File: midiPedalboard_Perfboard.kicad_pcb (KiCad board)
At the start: 8 copper layers, 66 x 50.8 mm, 49 parts, among them J1 wire, J10 wire, J11 wire, J12 wire, J13 wire, J14 wire, J15 MIDI_4, J16 MIDI_5, J17 MIDI_4, J18 MIDI_2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

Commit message: fix internal rst wire
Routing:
- net Net-(U1-PadRST): track 15.3 -> 16.3 mm
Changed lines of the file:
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@@
     (thickness 1.6)
     (drawings 6)
-    (tracks 135)
+    (tracks 139)
     (zones 0)
     (modules 49)
@@
   (layers
     (0 F.Cu signal)
-    (1 In1.Cu signal hide)
-    (2 In2.Cu signal hide)
+    (1 In1.Cu signal)
+    (2 In2.Cu signal)
     (3 wire1 signal)
     (4 wire2 signal)
-    (5 wire3 signal hide)
-    (6 wire4 signal hide)
+    (5 wire3 signal)
+    (6 wire4 signal)
     (31 B.Cu signal)
     (33 F.Adhes user)
@@
   )
   (setup
-    (last_trace_width 0.5)
+    (last_trace_width 0.25)
     (user_trace_width 0.25)
     (user_trace_width 0.5)
@@
   (segment (start 157.48 109.22) (end 157.48 111.180248) (width 0.25) (layer wire2) (net 27))
   (segment (start 160.02 113.720248) (end 160.02 114.3) (width 0.25) (layer wire2) (net 27))
-  (segment (start 144.999918 101.953781) (end 144.999918 86.697781) (width 0.5) (layer In1.Cu) (net 30))
+  (segment (start 144.78 86.344) (end 144.78 90.17) (width 0.25) (layer In1.Cu) (net 30))
+  (segment (start 144.78 90.17) (end 146.05 91.44) (width 0.25) (layer In1.Cu) (net 30))
+  (segment (start 146.05 91.44) (end 146.05 97.79) (width 0.25) (layer In1.Cu) (net 30))
+  (segment (start 144.78 99.06) (end 144.78 101.6) (width 0.25) (layer In1.Cu) (net 30))
+  (segment (start 146.05 97.79) (end 144.78 99.06) (width 0.25) (layer In1.Cu) (net 30))
   (segment (start 152.619918 86.697781) (end 150.079918 86.697781) (width 0.5) (layer In1.Cu) (net 31))
   (segment (start 149.86 81.28) (end 149.86 78.74) (width 0.5) (layer B.Cu) (net 37))

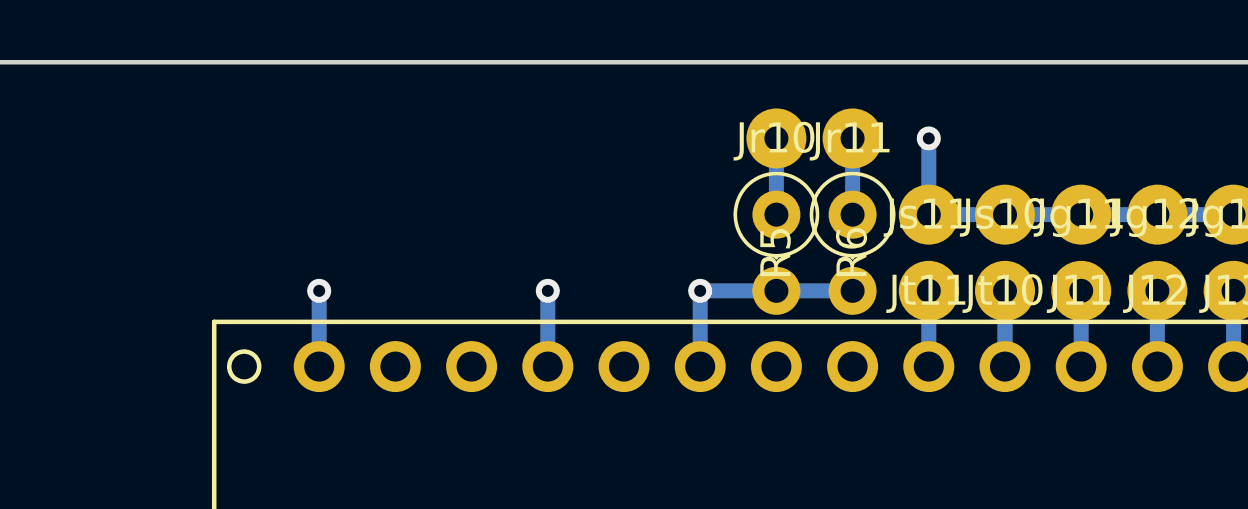
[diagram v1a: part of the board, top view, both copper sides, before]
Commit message: condensator for adc filtering
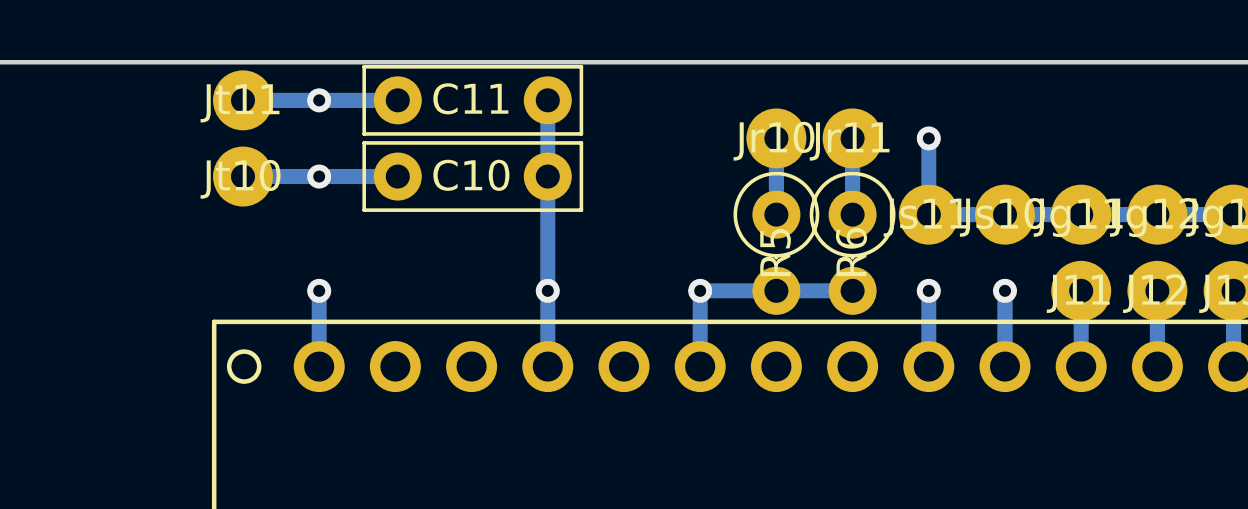
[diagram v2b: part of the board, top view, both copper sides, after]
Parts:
- added C10: 100n, Capacitor_THT:C_Rect_L7.0mm_W2.0mm_P5.00mm, F.Cu at (137.2, 80.0)
- added C11: 100n, Capacitor_THT:C_Rect_L7.0mm_W2.0mm_P5.00mm, F.Cu at (137.2, 77.5)
- moved Jt10 25.7 mm to (132.1, 80.0)
- moved Jt11 23.7 mm to (132.1, 77.5)
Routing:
- net /exp: track 2.52 -> 32.1 mm, vias 0 -> 2
- net /exp_2: track 2.52 -> 30.6 mm, vias 0 -> 2
- net GND: track 142.4 -> 148.8 mm
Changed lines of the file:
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@@
     (thickness 1.6)
     (drawings 6)
-    (tracks 139)
+    (tracks 162)
     (zones 0)
-    (modules 49)
+    (modules 51)
     (nets 40)
   )
@@
   )
   (setup
-    (last_trace_width 0.25)
+    (last_trace_width 0.5)
     (user_trace_width 0.25)
     (user_trace_width 0.5)
@@
   )
   (module Connector_Wire:SolderWirePad_1x01_Drill0.8mm (layer F.Cu)
-    (at 154.94 83.82 180)
+    (at 132.08 77.47 180)
     (descr "Wire solder connection")
     (tags connector)
@@
   )
   (module Connector_Wire:SolderWirePad_1x01_Drill0.8mm (layer F.Cu)
-    (at 157.48 83.82 180)
+    (at 132.08 80.01 180)
     (descr "Wire solder connection")
     (tags connector)
@@
     )
   )
+  (module Capacitor_THT:C_Rect_L7.0mm_W2.0mm_P5.00mm (layer F.Cu)
+    (at 137.24 80.01)
+    (descr "C, Rect series, Radial, pin pitch=5.00mm, , length*width=7*2mm^2, Capacitor")
+    (tags "C Rect series Radial pin pitch 5.00mm  length 7mm width 2mm Capacitor")
+    (fp_text reference C10 (at 2.46 -0.005001) (layer F.SilkS)
+      (effects (font (size 1 1) (thickness 0.15)))
+    )
+    (fp_text value 100n (at 2.5 2.25) (layer F.Fab)
+      (effects (font (size 1 1) (thickness 0.15)))
+    )
+    (fp_text user %R (at 2.5 0) (layer F.Fab)
+      (effects (font (size 1 1) (thickness 0.15)))
+    )
+    (fp_line (start 6.25 -1.25) (end -1.25 -1.25) (layer F.CrtYd) (width 0.05))
+    (fp_line (start 6.25 1.25) (end 6.25 -1.25) (layer F.CrtYd) (width 0.05))
+    (fp_line (start -1.25 1.25) (end 6.25 1.25) (layer F.CrtYd) (width 0.05))
+    (fp_line (start -1.25 -1.25) (end -1.25 1.25) (layer F.CrtYd) (width 0.05))
+    (fp_line (start 6.12 -1.12) (end 6.12 1.12) (layer F.SilkS) (width 0.12))
+    (fp_line (start -1.12 -1.12) (end -1.12 1.12) (layer F.SilkS) (width 0.12))
+    (fp_line (start -1.12 1.12) (end 6.12 1.12) (layer F.SilkS) (width 0.12))
+    (fp_line (start -1.12 -1.12) (end 6.12 -1.12) (layer F.SilkS) (width 0.12))
+    (fp_line (start 6 -1) (end -1 -1) (layer F.Fab) (width 0.1))
+    (fp_line (start 6 1) (end 6 -1) (layer F.Fab) (width 0.1))
+    (fp_line (start -1 1) (end 6 1) (layer F.Fab) (width 0.1))
+    (fp_line (start -1 -1) (end -1 1) (layer F.Fab) (width 0.1))
+    (pad 2 thru_hole circle (at 5 0) (size 1.6 1.6) (drill 0.8) (layers *.Cu *.Mask)
+      (net 2 GND))
+    (pad 1 thru_hole circle (at 0 0) (size 1.6 1.6) (drill 0.8) (layers *.Cu *.Mask)
+      (net 14 /exp))
+    (model ${KISYS3DMOD}/Capacitor_THT.3dshapes/C_Rect_L7.0mm_W2.0mm_P5.00mm.wrl
+      (at (xyz 0 0 0))
+      (scale (xyz 1 1 1))
+      (rotate (xyz 0 0 0))
+    )
+  )
+  (module Capacitor_THT:C_Rect_L7.0mm_W2.0mm_P5.00mm (layer F.Cu)
+    (at 137.24 77.47)
+    (descr "C, Rect series, Radial, pin pitch=5.00mm, , length*width=7*2mm^2, Capacitor")
+    (tags "C Rect series Radial pin pitch 5.00mm  length 7mm width 2mm Capacitor")
+    (fp_text reference C11 (at 2.46 -0.015001) (layer F.SilkS)
+      (effects (font (size 1 1) (thickness 0.15)))
+    )
+    (fp_text value 100n (at 2.5 2.25) (layer F.Fab)
+      (effects (font (size 1 1) (thickness 0.15)))
+    )
+    (fp_line (start -1 -1) (end -1 1) (layer F.Fab) (width 0.1))
+    (fp_line (start -1 1) (end 6 1) (layer F.Fab) (width 0.1))
+    (fp_line (start 6 1) (end 6 -1) (layer F.Fab) (width 0.1))
+    (fp_line (start 6 -1) (end -1 -1) (layer F.Fab) (width 0.1))
+    (fp_line (start -1.12 -1.12) (end 6.12 -1.12) (layer F.SilkS) (width 0.12))
+    (fp_line (start -1.12 1.12) (end 6.12 1.12) (layer F.SilkS) (width 0.12))
+    (fp_line (start -1.12 -1.12) (end -1.12 1.12) (layer F.SilkS) (width 0.12))
+    (fp_line (start 6.12 -1.12) (end 6.12 1.12) (layer F.SilkS) (width 0.12))
+    (fp_line (start -1.25 -1.25) (end -1.25 1.25) (layer F.CrtYd) (width 0.05))
+    (fp_line (start -1.25 1.25) (end 6.25 1.25) (layer F.CrtYd) (width 0.05))
+    (fp_line (start 6.25 1.25) (end 6.25 -1.25) (layer F.CrtYd) (width 0.05))
+    (fp_line (start 6.25 -1.25) (end -1.25 -1.25) (layer F.CrtYd) (width 0.05))
+    (fp_text user %R (at 2.5 0) (layer F.Fab)
+      (effects (font (size 1 1) (thickness 0.15)))
+    )
+    (pad 1 thru_hole circle (at 0 0) (size 1.6 1.6) (drill 0.8) (layers *.Cu *.Mask)
+      (net 39 /exp_2))
+    (pad 2 thru_hole circle (at 5 0) (size 1.6 1.6) (drill 0.8) (layers *.Cu *.Mask)
+      (net 2 GND))
+    (model ${KISYS3DMOD}/Capacitor_THT.3dshapes/C_Rect_L7.0mm_W2.0mm_P5.00mm.wrl
+      (at (xyz 0 0 0))
+      (scale (xyz 1 1 1))
+      (rotate (xyz 0 0 0))
+    )
+  )
   (gr_line (start 177.8 76.2) (end 177.8 127) (layer Edge.Cuts) (width 0.15))
   (gr_line (start 111.76 76.2) (end 177.8 76.2) (layer Edge.Cuts) (width 0.15))
@@
   (segment (start 162.56 116.84) (end 167.64 116.84) (width 0.5) (layer B.Cu) (net 2))
   (segment (start 167.64 116.84) (end 167.64 111.6) (width 0.5) (layer B.Cu) (net 2))
+  (segment (start 142.24 77.47) (end 142.24 83.82) (width 0.5) (layer B.Cu) (net 2))
   (segment (start 165.1 101.6) (end 165.1 104.14) (width 0.5) (layer B.Cu) (net 3))
   (segment (start 165.1 104.14) (end 165.1 106.68) (width 0.5) (layer B.Cu) (net 3))
@@
   (segment (start 170.18 101.6) (end 170.18 104.14) (width 0.5) (layer B.Cu) (net 13))
   (segment (start 157.48 86.344) (end 157.48 83.82) (width 0.5) (layer B.Cu) (net 14))
+  (segment (start 132.08 80.01) (end 134.62 80.01) (width 0.5) (layer B.Cu) (net 14))
+  (segment (start 134.62 80.01) (end 137.24 80.01) (width 0.5) (layer B.Cu) (net 14))
+  (via (at 134.62 80.01) (size 0.8) (drill 0.4) (layers F.Cu B.Cu) (net 14))
+  (segment (start 157.48 83.82) (end 157.48 83.82) (width 0.5) (layer B.Cu) (net 14))
+  (via (at 157.48 83.82) (size 0.8) (drill 0.4) (layers F.Cu B.Cu) (net 14))
+  (segment (start 156.354999 82.694999) (end 147.464999 82.694999) (width 0.25) (layer wire3) (net 14))
+  (segment (start 157.48 83.82) (end 156.354999 82.694999) (width 0.25) (layer wire3) (net 14))
+  (segment (start 147.464999 82.694999) (end 146.685 81.915) (width 0.25) (layer wire3) (net 14))
+  (segment (start 136.525 81.915) (end 134.62 80.01) (width 0.25) (layer wire3) (net 14))
+  (segment (start 146.685 81.915) (end 136.525 81.915) (width 0.25) (layer wire3) (net 14))
   (segment (start 160.02 86.344) (end 160.02 83.82) (width 0.5) (layer B.Cu) (net 15))
   (segment (start 162.56 86.344) (end 162.56 83.82) (width 0.5) (layer B.Cu) (net 16))
@@
   (segment (start 152.4 81.28) (end 152.4 78.74) (width 0.5) (layer B.Cu) (net 38))
   (segment (start 154.94 86.344) (end 154.94 83.82) (width 0.5) (layer B.Cu) (net 39))
+  (segment (start 132.08 77.47) (end 134.62 77.47) (width 0.5) (layer B.Cu) (net 39))
+  (segment (start 134.62 77.47) (end 137.24 77.47) (width 0.5) (layer B.Cu) (net 39))
+  (via (at 134.62 77.47) (size 0.8) (drill 0.4) (layers F.Cu B.Cu) (net 39))
+  (segment (start 154.94 83.82) (end 154.94 83.82) (width 0.5) (layer B.Cu) (net 39))
+  (via (at 154.94 83.82) (size 0.8) (drill 0.4) (layers F.Cu B.Cu) (net 39))
+  (segment (start 152.650003 82.405001) (end 147.810001 82.405001) (width 0.25) (layer wire4) (net 39))
+  (segment (start 154.065002 83.82) (end 152.650003 82.405001) (width 0.25) (layer wire4) (net 39))
+  (segment (start 154.94 83.82) (end 154.065002 83.82) (width 0.25) (layer wire4) (net 39))
+  (segment (start 135.019999 77.869999) (end 134.62 77.47) (width 0.25) (layer wire4) (net 39))
+  (segment (start 135.745001 78.595001) (end 135.019999 77.869999) (width 0.25) (layer wire4) (net 39))
+  (segment (start 144.000001 78.595001) (end 135.745001 78.595001) (width 0.25) (layer wire4) (net 39))
+  (segment (start 147.810001 82.405001) (end 144.000001 78.595001) (width 0.25) (layer wire4) (net 39))
 )

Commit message: revert order of fs pin to reflect what i really did
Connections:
- J21 pad 1: /fs_2 -> /fs_1
- J22 pad 1: /fs_3 -> /fs_0
- J8 pad 1: /fs_0 -> /fs_3
- J9 pad 1: /fs_1 -> /fs_2
- U1 pad 10: /fs_1 -> /fs_2
- U1 pad 11: /fs_2 -> /fs_1
- U1 pad 12: /fs_3 -> /fs_0
- U1 pad 9: /fs_0 -> /fs_3
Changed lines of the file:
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@@
   )
   (setup
-    (last_trace_width 0.5)
+    (last_trace_width 0.25)
     (user_trace_width 0.25)
     (user_trace_width 0.5)
@@
       (net 3 /rotary_b))
     (pad 9 thru_hole circle (at 36.52 -1.254) (size 1.7 1.7) (drill 1) (layers *.Cu *.Mask)
+      (net 24 /fs_3))
+    (pad 10 thru_hole circle (at 39.06 -1.254) (size 1.7 1.7) (drill 1) (layers *.Cu *.Mask)
+      (net 23 /fs_2))
+    (pad 11 thru_hole circle (at 41.6 -1.254) (size 1.7 1.7) (drill 1) (layers *.Cu *.Mask)
+      (net 13 /fs_1))
+    (pad 12 thru_hole circle (at 44.14 -1.254) (size 1.7 1.7) (drill 1) (layers *.Cu *.Mask)
       (net 12 /fs_0))
-    (pad 10 thru_hole circle (at 39.06 -1.254) (size 1.7 1.7) (drill 1) (layers *.Cu *.Mask)
-      (net 13 /fs_1))
-    (pad 11 thru_hole circle (at 41.6 -1.254) (size 1.7 1.7) (drill 1) (layers *.Cu *.Mask)
-      (net 23 /fs_2))
-    (pad 12 thru_hole circle (at 44.14 -1.254) (size 1.7 1.7) (drill 1) (layers *.Cu *.Mask)
-      (net 24 /fs_3))
   )
   (module MountingHole:MountingHole_4.3mm_M4 (layer F.Cu)
@@
     )
     (pad 1 thru_hole circle (at 0 0 180) (size 1.99898 1.99898) (drill 0.8001) (layers *.Cu *.Mask)
-      (net 12 /fs_0))
+      (net 24 /fs_3))
   )
   (module Connector_Wire:SolderWirePad_1x01_Drill0.8mm (layer F.Cu)
@@
     (fp_line (start 1.5 1.5) (end -1.5 1.5) (layer F.CrtYd) (width 0.05))
     (pad 1 thru_hole circle (at 0 0 180) (size 1.99898 1.99898) (drill 0.8001) (layers *.Cu *.Mask)
-      (net 13 /fs_1))
+      (net 23 /fs_2))
   )
   (module Connector_Wire:SolderWirePad_1x01_Drill0.8mm (layer F.Cu)
@@
     )
     (pad 1 thru_hole circle (at 0 0 180) (size 1.99898 1.99898) (drill 0.8001) (layers *.Cu *.Mask)
-      (net 23 /fs_2))
+      (net 13 /fs_1))
   )
   (module Connector_Wire:SolderWirePad_1x01_Drill0.8mm (layer F.Cu)
@@
     (fp_line (start 1.5 1.5) (end -1.5 1.5) (layer F.CrtYd) (width 0.05))
     (pad 1 thru_hole circle (at 0 0 180) (size 1.99898 1.99898) (drill 0.8001) (layers *.Cu *.Mask)
-      (net 24 /fs_3))
+      (net 12 /fs_0))
   )
   (module Resistor_THT:R_Axial_DIN0207_L6.3mm_D2.5mm_P2.54mm_Vertical (layer F.Cu)
@@
   (segment (start 157.48 101.6) (end 157.48 104.14) (width 0.5) (layer B.Cu) (net 10))
   (segment (start 160.02 101.6) (end 160.02 104.14) (width 0.5) (layer B.Cu) (net 11))
-  (segment (start 167.64 101.6) (end 167.64 104.14) (width 0.5) (layer B.Cu) (net 12))
-  (segment (start 170.18 101.6) (end 170.18 104.14) (width 0.5) (layer B.Cu) (net 13))
+  (segment (start 167.64 101.6) (end 167.64 104.14) (width 0.5) (layer B.Cu) (net 24))
+  (segment (start 170.18 101.6) (end 170.18 104.14) (width 0.5) (layer B.Cu) (net 23))
   (segment (start 157.48 86.344) (end 157.48 83.82) (width 0.5) (layer B.Cu) (net 14))
   (segment (start 132.08 80.01) (end 134.62 80.01) (width 0.5) (layer B.Cu) (net 14))
@@
   (segment (start 135.745001 105.265001) (end 143.365001 105.265001) (width 0.25) (layer wire1) (net 22))
   (segment (start 134.62 104.14) (end 135.745001 105.265001) (width 0.25) (layer wire1) (net 22))
-  (segment (start 172.72 101.6) (end 172.72 104.14) (width 0.5) (layer B.Cu) (net 23))
-  (segment (start 175.26 101.6) (end 175.26 104.14) (width 0.5) (layer B.Cu) (net 24))
+  (segment (start 172.72 101.6) (end 172.72 104.14) (width 0.5) (layer B.Cu) (net 13))
+  (segment (start 175.26 101.6) (end 175.26 104.14) (width 0.5) (layer B.Cu) (net 12))
   (segment (start 144.78 111.76) (end 144.78 109.22) (width 0.5) (layer B.Cu) (net 25))
   (via (at 144.78 109.22) (size 0.8) (drill 0.4) (layers F.Cu B.Cu) (net 25))
